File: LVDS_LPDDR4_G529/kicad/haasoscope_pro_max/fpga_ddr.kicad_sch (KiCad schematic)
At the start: 2 parts, among them U1 MT53D512M16D1DS_Aligned, U3 Ti90G529_Functions

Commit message: Aligned schematics, sort of
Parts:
- removed U3: Ti90G529_Functions, G529:BGA-529_23x23_19.0x19.0mm, symbol Ti90G529_Functions:Ti90G529_Functions
- added U3: Ti90G529_Functions, haasoscope_pro_adc_fpga_board:BGA-529_23x23_19.0x19.0mm, symbol Ti90G529_Functions:Ti90G529_Functions
- U1: footprint MT53D512M32D2DS-053 WT_D:IC_MT53D512M16D1DS-046_WT_D -> easyeda2kicad:WFBGA-200_L14.5-W10.0-BL_MT53D512M32D2DS
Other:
- moved on the sheet: U1A

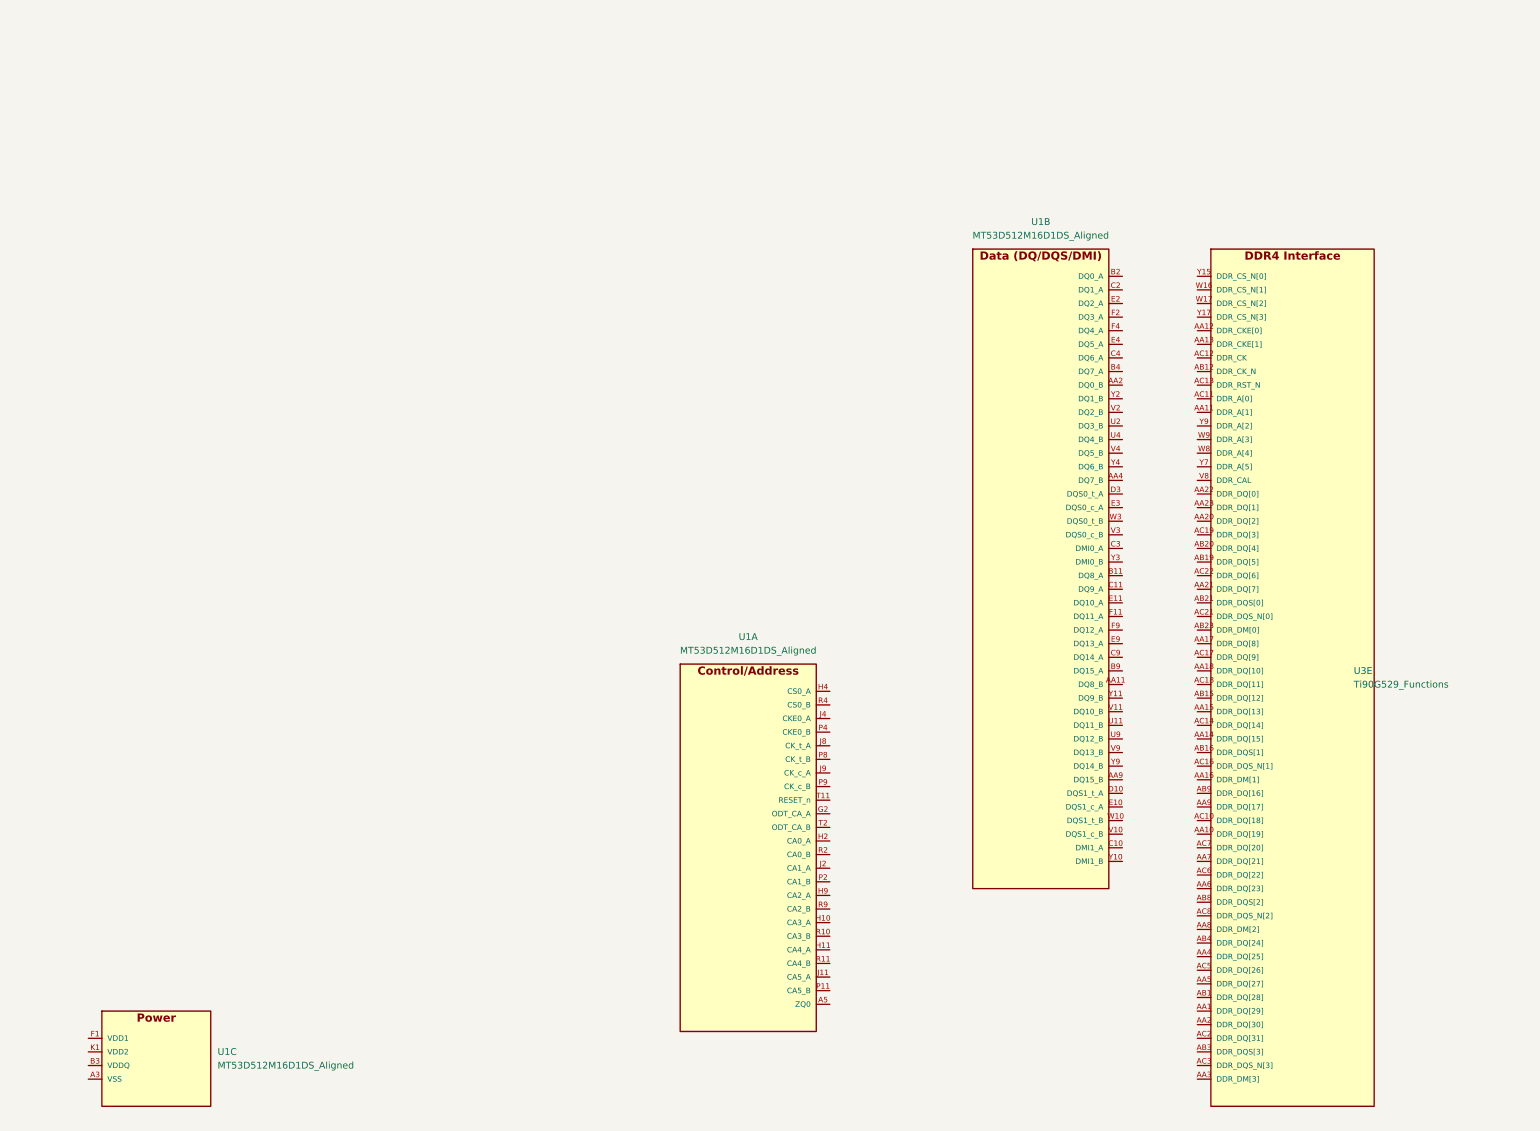
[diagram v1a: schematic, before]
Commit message: Aligned schematics, better
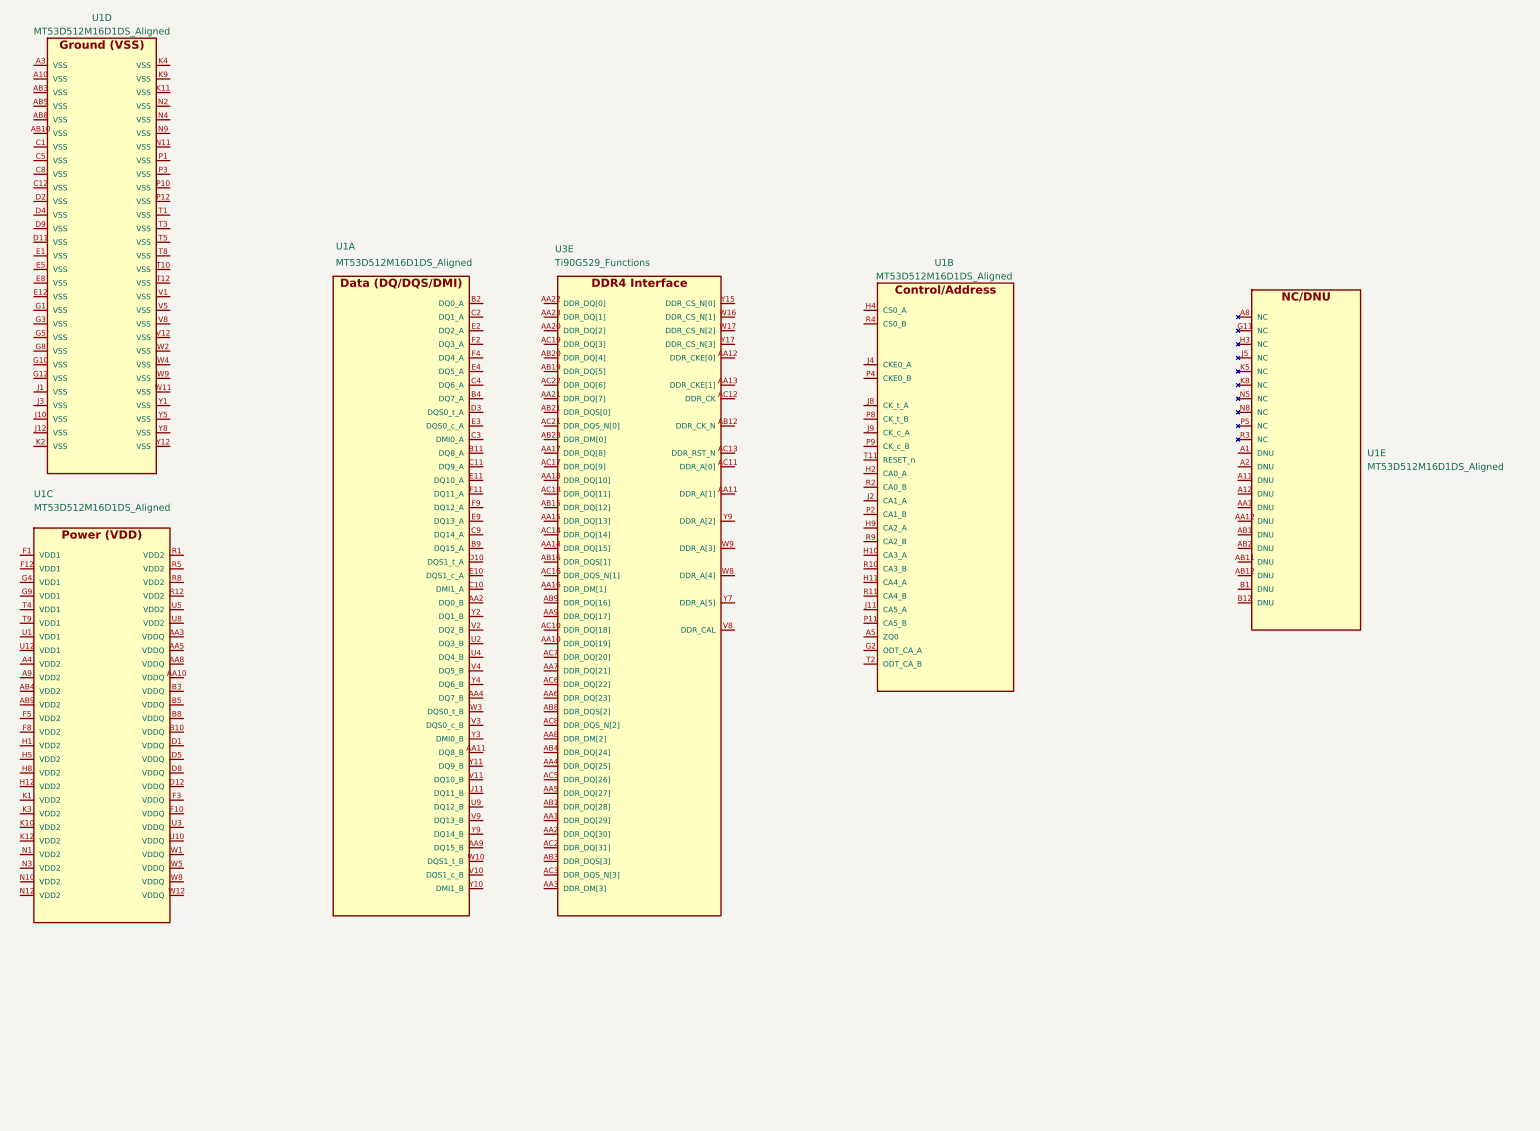
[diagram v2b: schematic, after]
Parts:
- added unit 5 of U1
- added unit 4 of U1
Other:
- moved on the sheet: U3E

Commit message: Aligned schematics, connected some components
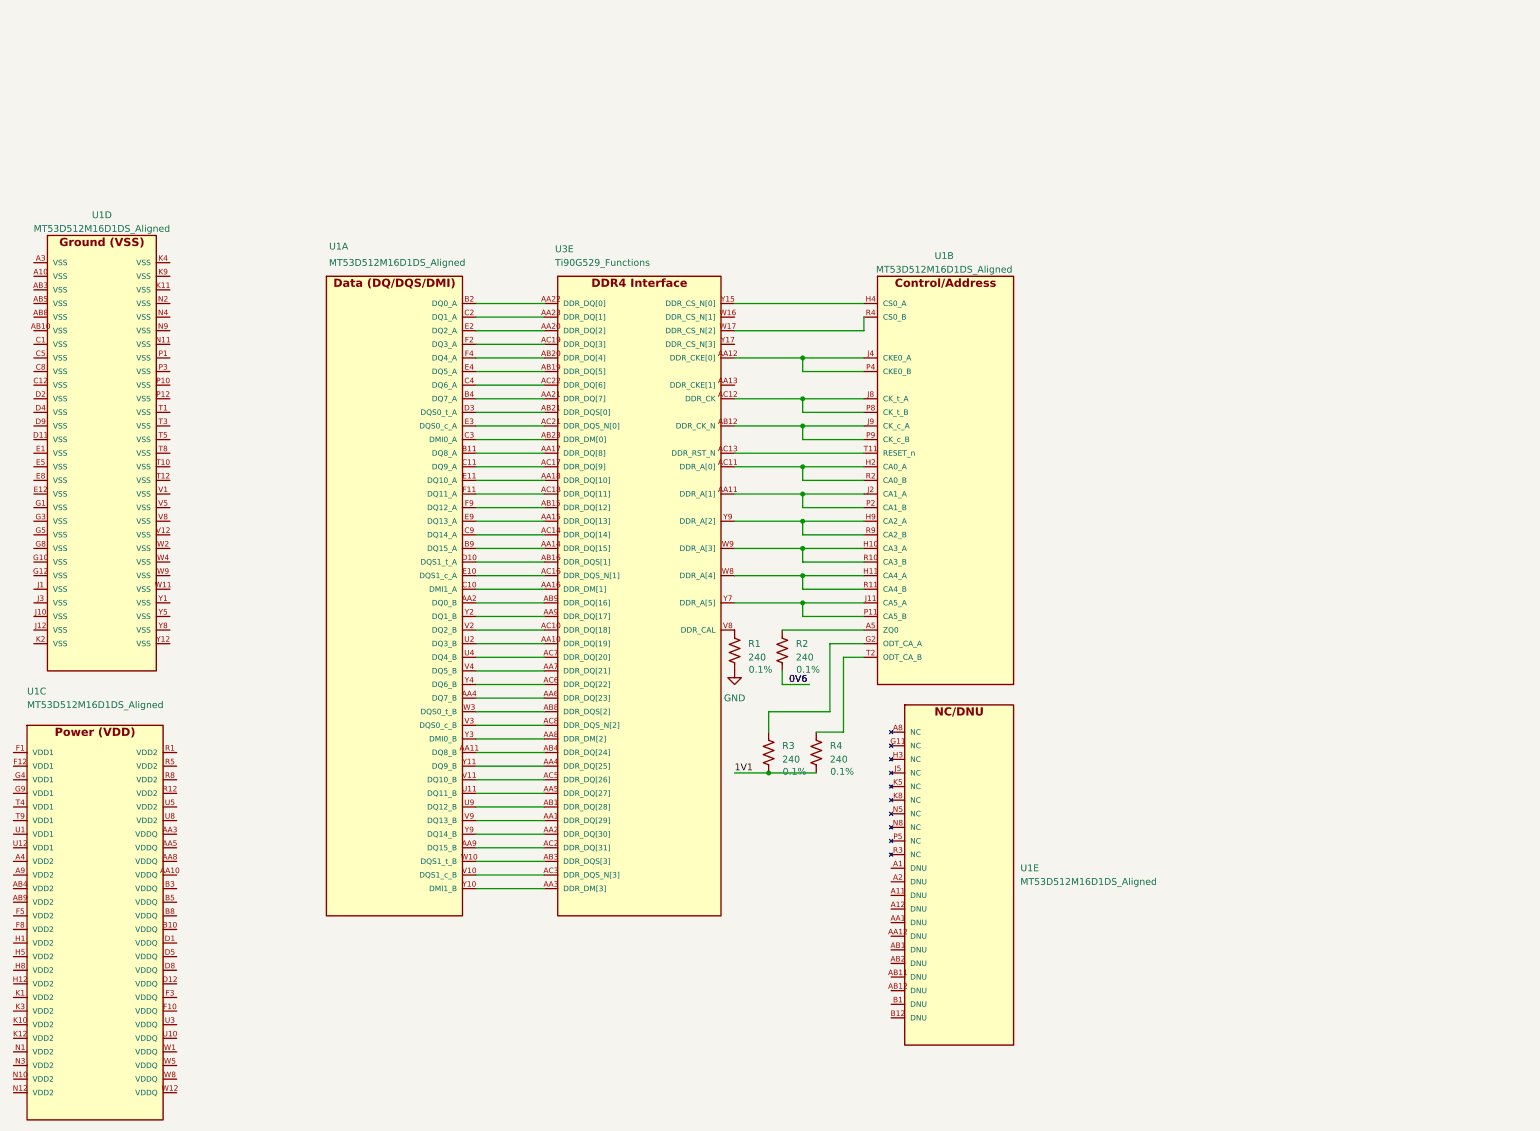
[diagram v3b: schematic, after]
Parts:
- added R1, R2, R3, R4: 240, Resistor_SMD:R_0402_1005Metric, symbol Device:R_US
- U1: footprint easyeda2kicad:WFBGA-200_L14.5-W10.0-BL_MT53D512M32D2DS -> MT53D512M32D2DS-053 WT_D:IC_MT53D512M16D1DS-046_WT_D
- U3: footprint haasoscope_pro_adc_fpga_board:BGA-529_23x23_19.0x19.0mm -> G529:BGA-529_23x23_19.0x19.0mm
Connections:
- net at U1.A5 (ZQ0): now also R2.1
- net at U1.G2 (ODT_CA_A): now also R3.1
- net at U1.H10 (CA3_A): now also U1.R10 (CA3_B), U3.W9 (DDR_A[3])
- net at U1.H11 (CA4_A): now also U1.R11 (CA4_B), U3.W8 (DDR_A[4])
- net at U1.H2 (CA0_A): now also U1.R2 (CA0_B), U3.AC11 (DDR_A[0])
- net at U1.H4 (CS0_A): now also U3.Y15 (DDR_CS_N[0])
- net at U1.H9 (CA2_A): now also U1.R9 (CA2_B), U3.Y9 (DDR_A[2])
- net at U1.J11 (CA5_A): now also U1.P11 (CA5_B), U3.Y7 (DDR_A[5])
- net at U1.J2 (CA1_A): now also U1.P2 (CA1_B), U3.AA11 (DDR_A[1])
- net at U1.J4 (CKE0_A): now also U1.P4 (CKE0_B), U3.AA12 (DDR_CKE[0])
- net at U1.J8 (CK_t_A): now also U1.P8 (CK_t_B), U3.AC12 (DDR_CK)
- net at U1.J9 (CK_c_A): now also U1.P9 (CK_c_B), U3.AB12 (DDR_CK_N)
- net at U1.R4 (CS0_B): now also U3.W17 (DDR_CS_N[2])
- net at U1.T11 (RESET_n): now also U3.AC13 (DDR_RST_N)
- net at U1.T2 (ODT_CA_B): now also R4.1
- net at U1.AA11 (DQ8_B): now also U3.AB4 (DDR_DQ[24])
- net at U1.AA2 (DQ0_B): now also U3.AB9 (DDR_DQ[16])
- net at U1.AA4 (DQ7_B): now also U3.AA6 (DDR_DQ[23])
- net at U1.AA9 (DQ15_B): now also U3.AC2 (DDR_DQ[31])
- net at U1.B11 (DQ8_A): now also U3.AA17 (DDR_DQ[8])
- net at U1.B2 (DQ0_A): now also U3.AA22 (DDR_DQ[0])
- net at U1.B4 (DQ7_A): now also U3.AA21 (DDR_DQ[7])
- net at U1.B9 (DQ15_A): now also U3.AA14 (DDR_DQ[15])
- net at U1.C10 (DMI1_A): now also U3.AA16 (DDR_DM[1])
- net at U1.C11 (DQ9_A): now also U3.AC17 (DDR_DQ[9])
- net at U1.C2 (DQ1_A): now also U3.AA23 (DDR_DQ[1])
- net at U1.C3 (DMI0_A): now also U3.AB23 (DDR_DM[0])
- net at U1.C4 (DQ6_A): now also U3.AC22 (DDR_DQ[6])
- net at U1.C9 (DQ14_A): now also U3.AC14 (DDR_DQ[14])
- net at U1.D10 (DQS1_t_A): now also U3.AB16 (DDR_DQS[1])
- net at U1.D3 (DQS0_t_A): now also U3.AB21 (DDR_DQS[0])
- net at U1.E10 (DQS1_c_A): now also U3.AC16 (DDR_DQS_N[1])
- net at U1.E11 (DQ10_A): now also U3.AA18 (DDR_DQ[10])
- net at U1.E2 (DQ2_A): now also U3.AA20 (DDR_DQ[2])
- net at U1.E3 (DQS0_c_A): now also U3.AC21 (DDR_DQS_N[0])
- net at U1.E4 (DQ5_A): now also U3.AB19 (DDR_DQ[5])
- net at U1.E9 (DQ13_A): now also U3.AA15 (DDR_DQ[13])
- net at U1.F11 (DQ11_A): now also U3.AC18 (DDR_DQ[11])
- net at U1.F2 (DQ3_A): now also U3.AC19 (DDR_DQ[3])
- net at U1.F4 (DQ4_A): now also U3.AB20 (DDR_DQ[4])
- net at U1.F9 (DQ12_A): now also U3.AB15 (DDR_DQ[12])
- net at U1.U11 (DQ11_B): now also U3.AA5 (DDR_DQ[27])
- net at U1.U2 (DQ3_B): now also U3.AA10 (DDR_DQ[19])
- net at U1.U4 (DQ4_B): now also U3.AC7 (DDR_DQ[20])
- net at U1.U9 (DQ12_B): now also U3.AB1 (DDR_DQ[28])
- net at U1.V10 (DQS1_c_B): now also U3.AC3 (DDR_DQS_N[3])
- net at U1.V11 (DQ10_B): now also U3.AC5 (DDR_DQ[26])
- net at U1.V2 (DQ2_B): now also U3.AC10 (DDR_DQ[18])
- net at U1.V3 (DQS0_c_B): now also U3.AC8 (DDR_DQS_N[2])
- net at U1.V4 (DQ5_B): now also U3.AA7 (DDR_DQ[21])
- net at U1.V9 (DQ13_B): now also U3.AA1 (DDR_DQ[29])
- net at U1.W10 (DQS1_t_B): now also U3.AB3 (DDR_DQS[3])
- net at U1.W3 (DQS0_t_B): now also U3.AB8 (DDR_DQS[2])
- net at U1.Y10 (DMI1_B): now also U3.AA3 (DDR_DM[3])
- net at U1.Y11 (DQ9_B): now also U3.AA4 (DDR_DQ[25])
- net at U1.Y2 (DQ1_B): now also U3.AA9 (DDR_DQ[17])
- net at U1.Y3 (DMI0_B): now also U3.AA8 (DDR_DM[2])
- net at U1.Y4 (DQ6_B): now also U3.AC6 (DDR_DQ[22])
- net at U1.Y9 (DQ14_B): now also U3.AA2 (DDR_DQ[30])
- net at U3.V8 (DDR_CAL): now also R1.1
- new net 0V6: R2.2
- new net 1V1: R3.2, R4.2
- new net GND: R1.2
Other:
- moved on the sheet: U1A, U1B, U1C, U1D, U1E
